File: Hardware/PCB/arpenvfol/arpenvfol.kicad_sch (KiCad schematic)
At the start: 76 parts, among them J1 AudioJack2_SwitchT, J10 3_pin_Molex_header, J11 AudioJack2, J12 AudioJack2, J2 AudioJack2_SwitchT, J3 Synth_power_2x5, J4 AudioJack2_SwitchT, J5 2_pin_Molex_connector, J6 2_pin_Molex_connector, J7 3_pin_Molex_connector, J8 2_pin_Molex_header, J9 2_pin_Molex_header, Q1 BC549, Q2 BC549, U1 TL074

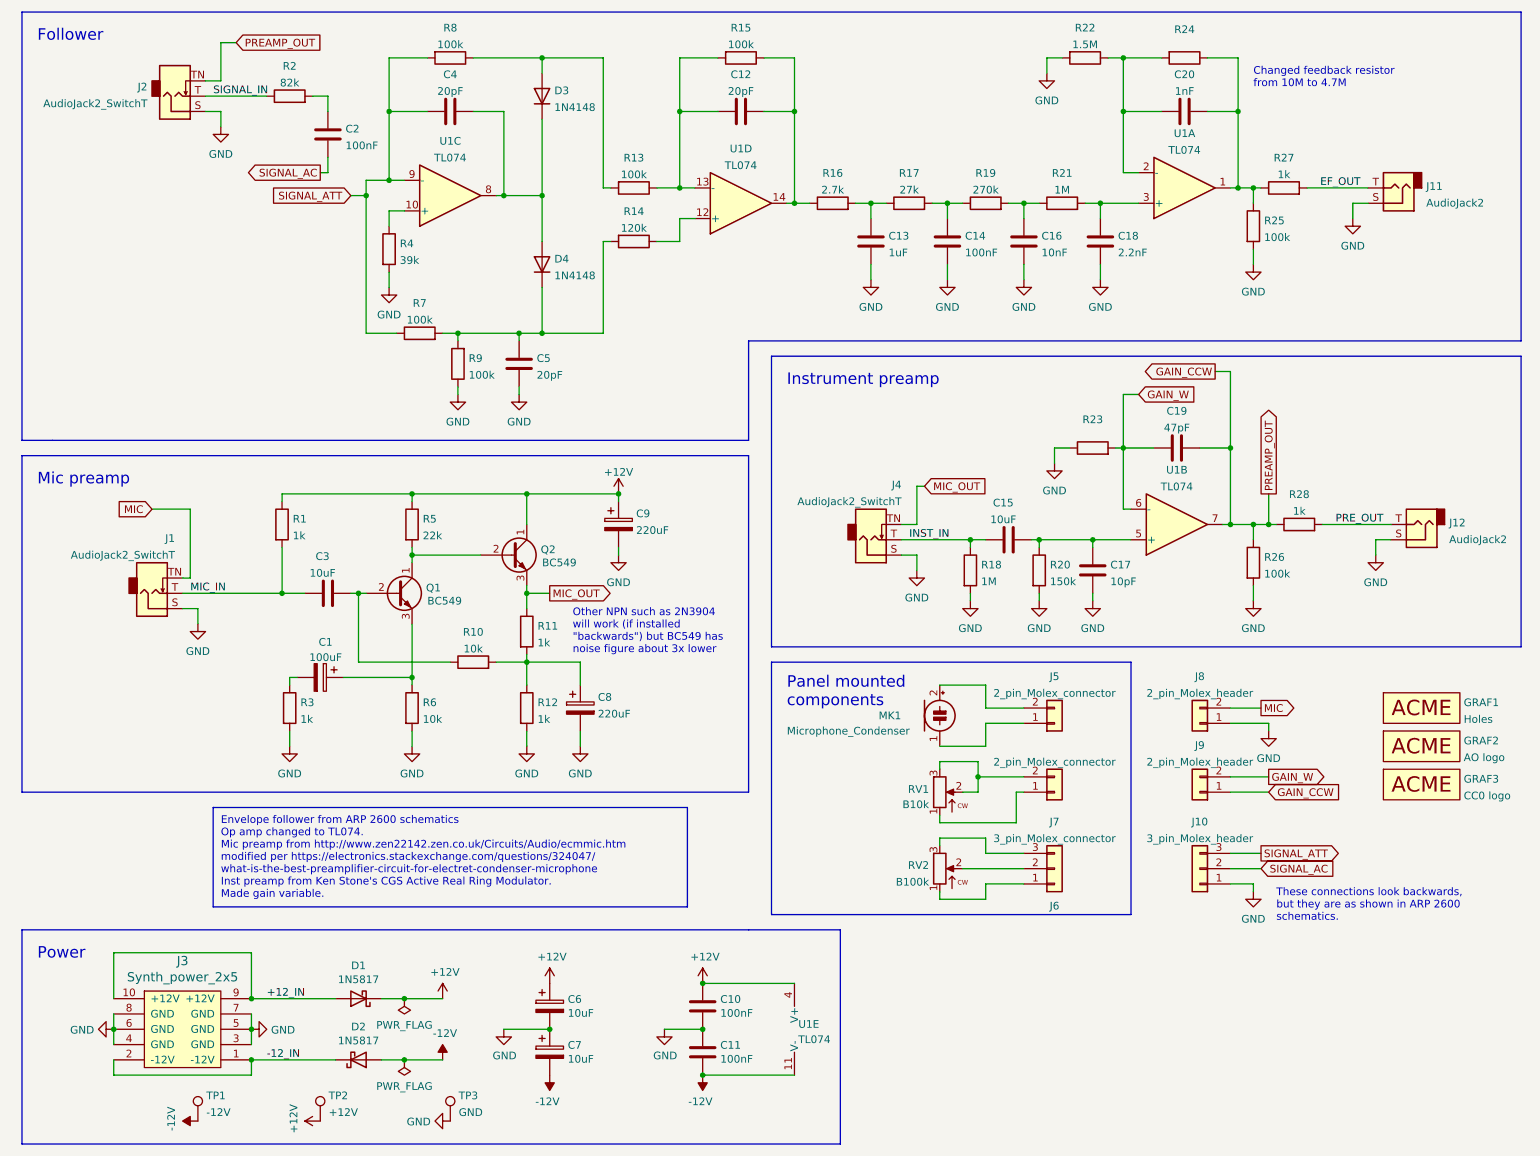
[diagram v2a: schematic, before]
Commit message: Revert "Change 2 resistor values"
This reverts commit a172cd43ee9637b883d7b4f7545da2461ae37f05.
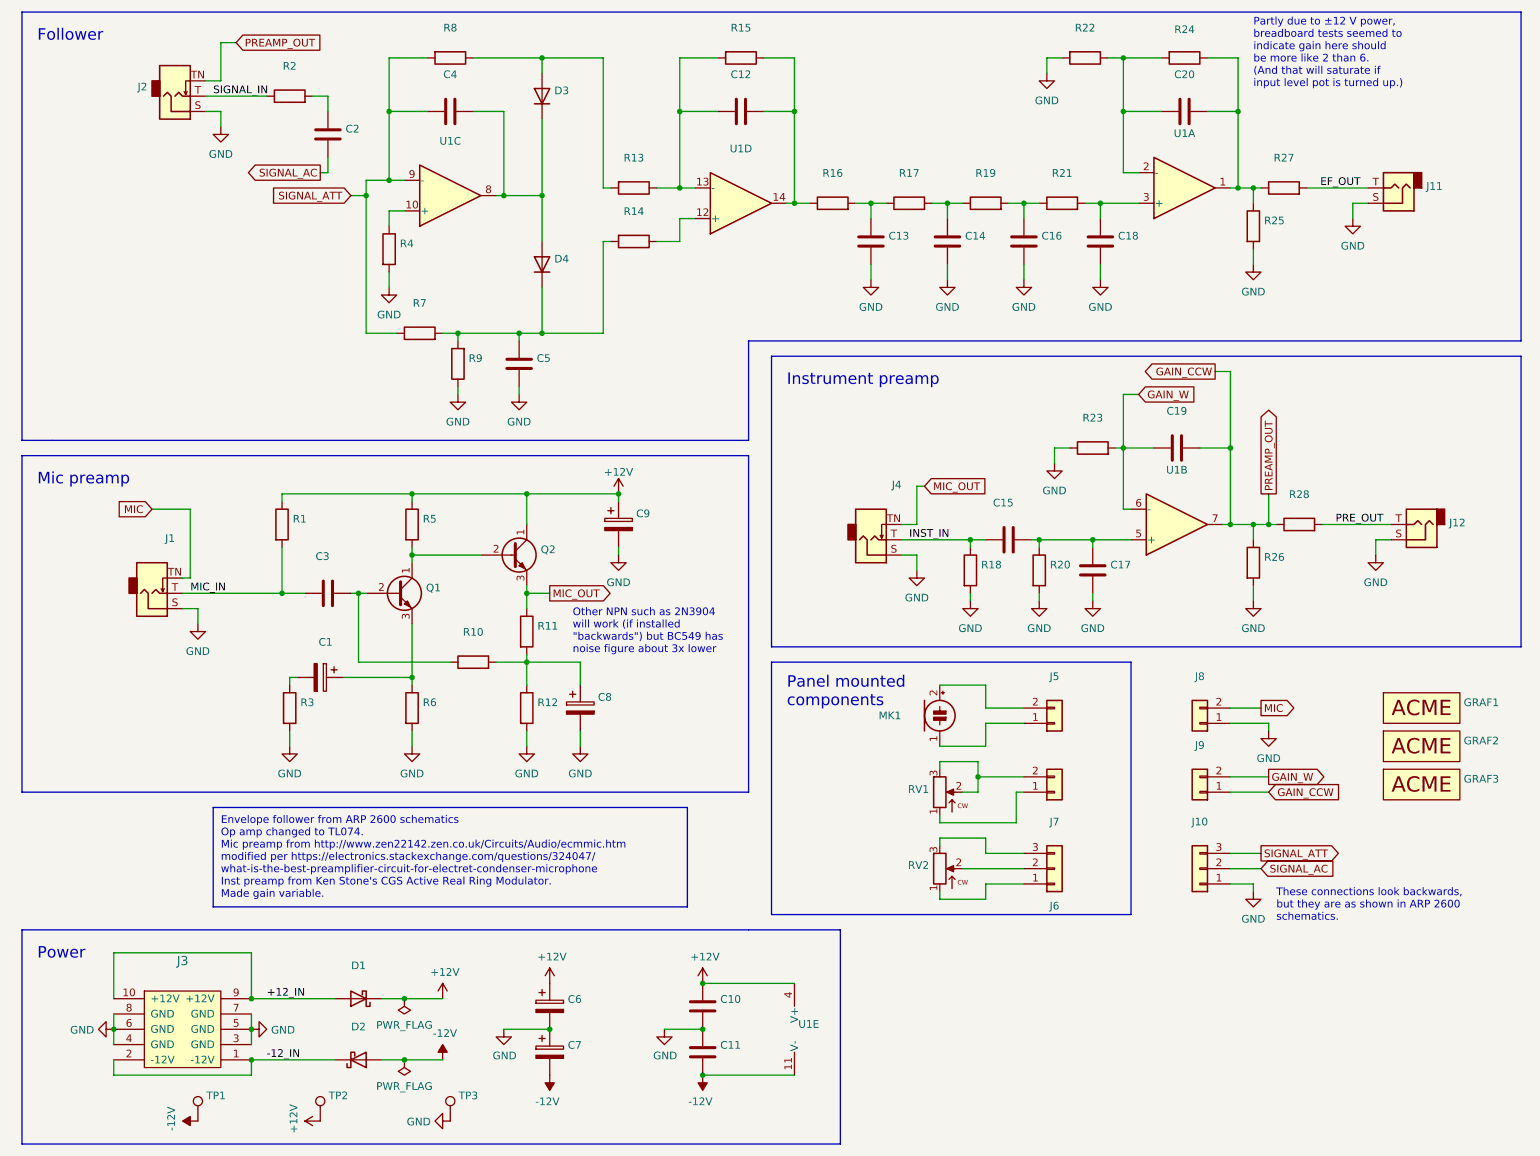
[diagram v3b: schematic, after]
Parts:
- C1: value 100uF -> (none); footprint ao_tht:CP_Radial_D6.3mm_P2.50mm -> (none)
- C10, C11: value 100nF -> (none); footprint ao_tht:C_Disc_D3.0mm_W1.6mm_P2.50mm -> (none)
- C12, C4, C5: value 20pF -> (none); footprint ao_tht:C_Disc_D5.0mm_W2.5mm_P5.00mm -> (none)
- C13: value 1uF -> (none); footprint ao_tht:C_Rect_L7.2mm_W7.2mm_P5.00mm_FKS2_FKP2_MKS2_MKP2 -> (none)
- C14, C2: value 100nF -> (none); footprint ao_tht:C_Rect_L7.2mm_W2.5mm_P5.00mm_FKS2_FKP2_MKS2_MKP2 -> (none)
- C15, C3: value 10uF -> (none); footprint ao_tht:C_Radial_D8.0mm_H11.5mm_P3.50mm -> (none)
- C16: value 10nF -> (none); footprint ao_tht:C_Rect_L7.2mm_W2.5mm_P5.00mm_FKS2_FKP2_MKS2_MKP2 -> (none)
- C17: value 10pF -> (none); footprint ao_tht:C_Disc_D5.0mm_W2.5mm_P5.00mm -> (none)
- C18: value 2.2nF -> (none); footprint ao_tht:C_Rect_L7.2mm_W2.5mm_P5.00mm_FKS2_FKP2_MKS2_MKP2 -> (none)
- C19: value 47pF -> (none); footprint ao_tht:C_Disc_D5.0mm_W2.5mm_P5.00mm -> (none)
- C20: value 1nF -> (none); footprint ao_tht:C_Rect_L7.2mm_W2.5mm_P5.00mm_FKS2_FKP2_MKS2_MKP2 -> (none)
- C6, C7: value 10uF -> (none); footprint ao_tht:CP_Radial_D6.3mm_P2.50mm -> (none)
- C8, C9: value 220uF -> (none); footprint ao_tht:CP_Radial_D6.3mm_P2.50mm -> (none)
- D1, D2: value 1N5817 -> (none); footprint ao_tht:D_DO-41_SOD81_P10.16mm_Horizontal -> (none)
- D3, D4: value 1N4148 -> (none); footprint ao_tht:D_DO-35_SOD27_P7.62mm_Horizontal -> (none)
- GRAF1: value Holes -> (none); footprint arpenvfol:arpenvfol_panel_holes -> (none)
- GRAF2: value AO logo -> (none); footprint ao_tht:analogoutput_12mm -> (none)
- GRAF3: value CC0 logo -> (none); footprint ao_tht:CC0_logo -> (none)
- J1, J2, J4: value AudioJack2_SwitchT -> (none); footprint ao_tht:Jack_6.35mm_PJ_629HAN_slots -> (none)
- J10: value 3_pin_Molex_header -> (none); footprint ao_tht:Molex_KK-254_AE-6410-03A_1x03_P2.54mm_Vertical -> (none)
- J11, J12: value AudioJack2 -> (none); footprint ao_tht:Jack_6.35mm_PJ_629HAN_slots -> (none)
- J3: value Synth_power_2x5 -> (none); footprint ao_tht:Power_Header -> (none)
- J5, J6: value 2_pin_Molex_connector -> (none); footprint ao_tht:Molex_KK-254_AE-6410-02A_1x02_P2.54mm_Vertical -> (none)
- J7: value 3_pin_Molex_connector -> (none); footprint ao_tht:Molex_KK-254_AE-6410-03A_1x03_P2.54mm_Vertical -> (none)
- J8, J9: value 2_pin_Molex_header -> (none); footprint ao_tht:Molex_KK-254_AE-6410-02A_1x02_P2.54mm_Vertical -> (none)
- MK1: value Microphone_Condenser -> (none)
- Q1, Q2: value BC549 -> (none); footprint ao_tht:TO-92_Inline_Wide -> (none)
- R1, R11, R12, R27, R28, R3: value 1k -> (none); footprint ao_tht:R_Axial_DIN0207_L6.3mm_D2.5mm_P10.16mm_Horizontal -> (none)
- R10, R6: value 10k -> (none); footprint ao_tht:R_Axial_DIN0207_L6.3mm_D2.5mm_P10.16mm_Horizontal -> (none)
- R13, R15, R25, R26, R7, R8, R9: value 100k -> (none); footprint ao_tht:R_Axial_DIN0207_L6.3mm_D2.5mm_P10.16mm_Horizontal -> (none)
- R14: value 120k -> (none); footprint ao_tht:R_Axial_DIN0207_L6.3mm_D2.5mm_P10.16mm_Horizontal -> (none)
- R16: value 2.7k -> (none); footprint ao_tht:R_Axial_DIN0207_L6.3mm_D2.5mm_P10.16mm_Horizontal -> (none)
- R17: value 27k -> (none); footprint ao_tht:R_Axial_DIN0207_L6.3mm_D2.5mm_P10.16mm_Horizontal -> (none)
- R18, R21: value 1M -> (none); footprint ao_tht:R_Axial_DIN0207_L6.3mm_D2.5mm_P10.16mm_Horizontal -> (none)
- R19: value 270k -> (none); footprint ao_tht:R_Axial_DIN0207_L6.3mm_D2.5mm_P10.16mm_Horizontal -> (none)
- R2: value 82k -> (none); footprint ao_tht:R_Axial_DIN0207_L6.3mm_D2.5mm_P10.16mm_Horizontal -> (none)
- R20: value 150k -> (none); footprint ao_tht:R_Axial_DIN0207_L6.3mm_D2.5mm_P10.16mm_Horizontal -> (none)
- R22: value 1.5M -> (none); footprint ao_tht:R_Axial_DIN0207_L6.3mm_D2.5mm_P10.16mm_Horizontal -> (none)
- R23, R24: footprint ao_tht:R_Axial_DIN0207_L6.3mm_D2.5mm_P10.16mm_Horizontal -> (none)
- R4: value 39k -> (none); footprint ao_tht:R_Axial_DIN0207_L6.3mm_D2.5mm_P10.16mm_Horizontal -> (none)
- R5: value 22k -> (none); footprint ao_tht:R_Axial_DIN0207_L6.3mm_D2.5mm_P10.16mm_Horizontal -> (none)
- RV1: value B10k -> (none)
- RV2: value B100k -> (none)
- TP1: value -12V -> (none); footprint ao_tht:TestPoint_THTPad_D1.5mm_Drill0.7mm -> (none)
- TP2: value +12V -> (none); footprint ao_tht:TestPoint_THTPad_D1.5mm_Drill0.7mm -> (none)
- TP3: value GND -> (none); footprint ao_tht:TestPoint_THTPad_1.5x1.5mm_Drill0.7mm -> (none)
- U1: value TL074 -> (none); footprint ao_tht:DIP-14_W7.62mm_Socket_LongPads -> (none)
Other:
- note added: "Partly due to ±12 V power, breadboard tests seemed to indicate gain here should be more like 2 than 6. (And that will saturate if input level pot is turned up.)"
- note removed: "Changed feedback resistor from 10M to 4.7M"
